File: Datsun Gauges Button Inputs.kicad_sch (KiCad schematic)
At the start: 13 parts, among them SW1 SW_Push, SW2 SW_Push, U1 4049, U2 4049

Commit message: Updated kicad diagrams
Updated kicad diagrams
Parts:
- removed D2: 1N4148, Diode_THT:D_DO-35_SOD27_P7.62mm_Horizontal, symbol Diode:1N4148
- added D2: 1N4734A 5.6v, Diode_THT:D_DO-41_SOD81_P10.16mm_Horizontal, symbol Diode:1N47xxA
- added D3: 1N4148, Diode_THT:D_DO-35_SOD27_P7.62mm_Horizontal, symbol Diode:1N4148
- R3, R4: value 10k -> 2k
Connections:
- net GND: now also D2.2 (A)
- net Park Brake Sw: now also D3.2 (A)
- net VCC: no longer R3.1
- net at C1.1, R4.1, U1.5: now also D2.1 (K), D3.1 (K)
- new net VDD: R3.1

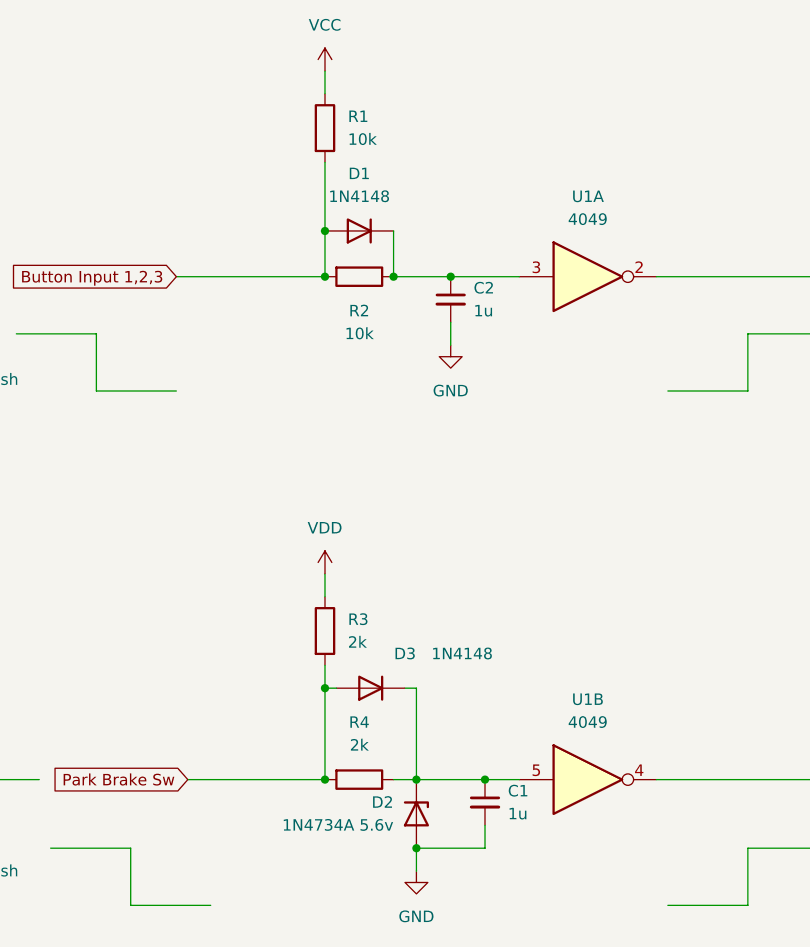
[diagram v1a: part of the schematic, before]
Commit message: Fixes
Changed some switch debouncing
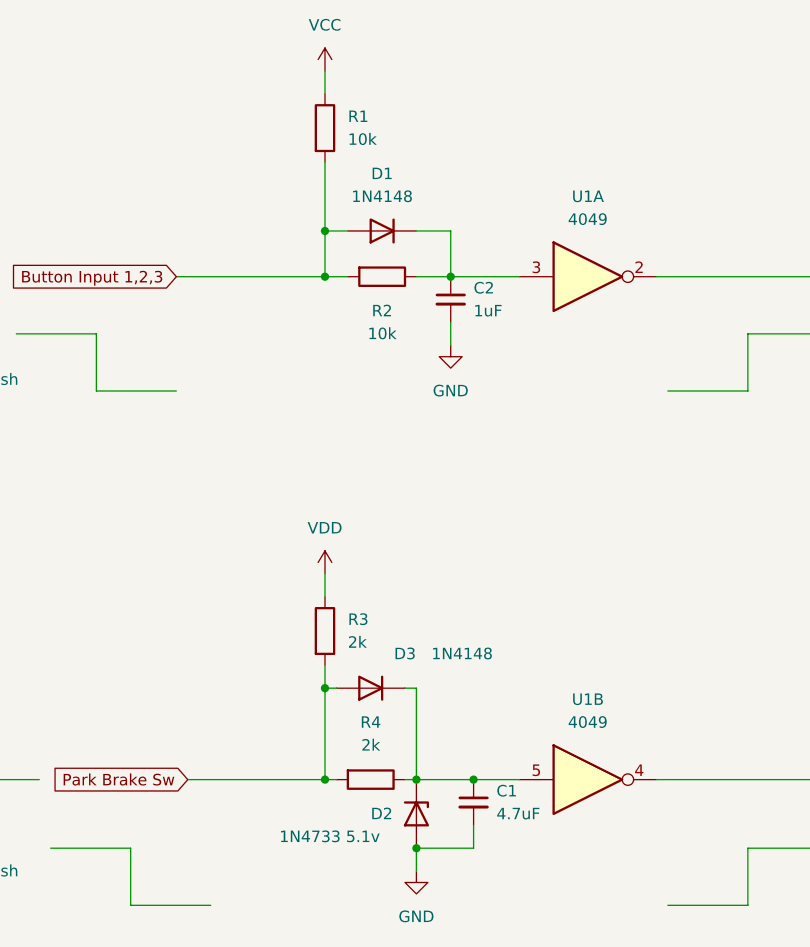
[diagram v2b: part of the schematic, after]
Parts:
- C1: value 1u -> 4.7uF
- C2: value 1u -> 1uF
- D2: value 1N4734A 5.6v -> 1N4733 5.1v
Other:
- moved on the sheet: C1, D1, R2, R4
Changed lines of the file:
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@@
   (junction (at 119.38 76.2) (diameter 0) (color 0 0 0 0)
   )
-  (junction (at 137.16 132.08) (diameter 0) (color 0 0 0 0)
-  )
   (junction (at 119.38 132.08) (diameter 0) (color 0 0 0 0)
   )
@@
   (junction (at 129.54 139.7) (diameter 0) (color 0 0 0 0)
   )
-  (junction (at 127 76.2) (diameter 0) (color 0 0 0 0)
+  (junction (at 135.89 132.08) (diameter 0) (color 0 0 0 0)
   )
   (junction (at 119.38 121.92) (diameter 0) (color 0 0 0 0)
@@
     (stroke (width 0) (type default))
   )
+  (wire (pts (xy 133.35 71.12) (xy 129.54 71.12))
+    (stroke (width 0) (type default))
+  )
   (wire (pts (xy 156.21 76.2) (xy 175.26 76.2))
     (stroke (width 0) (type default))
   )
-  (wire (pts (xy 137.16 137.16) (xy 137.16 139.7))
+  (wire (pts (xy 135.89 137.16) (xy 135.89 139.7))
     (stroke (width 0) (type default))
   )
@@
     (stroke (width 0) (type default) (color 0 0 255 1))
   )
-  (wire (pts (xy 127 71.12) (xy 127 76.2))
+  (wire (pts (xy 133.35 71.12) (xy 133.35 76.2))
     (stroke (width 0) (type default))
   )
@@
     (stroke (width 0) (type default) (color 0 0 255 1))
   )
-  (wire (pts (xy 127 132.08) (xy 129.54 132.08))
-    (stroke (width 0) (type default))
-  )
-  (wire (pts (xy 127 76.2) (xy 133.35 76.2))
-    (stroke (width 0) (type default))
-  )
   (wire (pts (xy 129.54 121.92) (xy 129.54 132.08))
     (stroke (width 0) (type default))
@@
     (stroke (width 0) (type default))
   )
+  (wire (pts (xy 135.89 132.08) (xy 140.97 132.08))
+    (stroke (width 0) (type default))
+  )
+  (wire (pts (xy 121.92 71.12) (xy 119.38 71.12))
+    (stroke (width 0) (type default))
+  )
+  (wire (pts (xy 133.35 76.2) (xy 129.54 76.2))
+    (stroke (width 0) (type default))
+  )
   (wire (pts (xy 228.6 34.29) (xy 228.6 25.4))
     (stroke (width 0) (type default))
@@
     (stroke (width 0) (type default))
   )
-  (wire (pts (xy 129.54 139.7) (xy 137.16 139.7))
+  (wire (pts (xy 129.54 139.7) (xy 135.89 139.7))
     (stroke (width 0) (type default))
   )
@@
     (stroke (width 0) (type default) (color 0 0 255 1))
   )
-  (wire (pts (xy 129.54 132.08) (xy 137.16 132.08))
+  (wire (pts (xy 129.54 132.08) (xy 135.89 132.08))
+    (stroke (width 0) (type default))
+  )
+  (wire (pts (xy 128.27 132.08) (xy 129.54 132.08))
     (stroke (width 0) (type default))
   )
@@
     (stroke (width 0) (type default))
   )
-  (wire (pts (xy 137.16 132.08) (xy 140.97 132.08))
+  (wire (pts (xy 121.92 76.2) (xy 119.38 76.2))
     (stroke (width 0) (type default))
   )
@@
   )
   (wire (pts (xy 119.38 109.22) (xy 119.38 111.76))
+    (stroke (width 0) (type default))
+  )
+  (wire (pts (xy 120.65 132.08) (xy 119.38 132.08))
     (stroke (width 0) (type default))
   )
@@
     )
   )
-  (symbol (lib_id "Device:C_Small") (at 137.16 134.62 0) (unit 1)
-    (in_bom yes) (on_board yes) (dnp no) (fields_autoplaced)
-    (property "Reference" "C1" (at 139.7 133.3563 0)
-      (effects (font (size 1.27 1.27)) (justify left))
-    )
-    (property "Value" "1u" (at 139.7 135.8963 0)
-      (effects (font (size 1.27 1.27)) (justify left))
-    )
-    (property "Footprint" "" (at 137.16 134.62 0)
-      (effects (font (size 1.27 1.27)) hide)
-    )
-    (property "Datasheet" "~" (at 137.16 134.62 0)
+  (symbol (lib_id "Device:C_Small") (at 135.89 134.62 0) (unit 1)
+    (in_bom yes) (on_board yes) (dnp no) (fields_autoplaced)
+    (property "Reference" "C1" (at 138.43 133.3563 0)
+      (effects (font (size 1.27 1.27)) (justify left))
+    )
+    (property "Value" "4.7uF" (at 138.43 135.8963 0)
+      (effects (font (size 1.27 1.27)) (justify left))
+    )
+    (property "Footprint" "" (at 135.89 134.62 0)
+      (effects (font (size 1.27 1.27)) hide)
+    )
+    (property "Datasheet" "~" (at 135.89 134.62 0)
       (effects (font (size 1.27 1.27)) hide)
     )
@@
   )
   (symbol (lib_id "Diode:1N47xxA") (at 129.54 135.89 270) (unit 1)
-    (in_bom yes) (on_board yes) (dnp no) (fields_autoplaced)
-    (property "Reference" "D2" (at 127 134.62 90)
-      (effects (font (size 1.27 1.27)) (justify right))
-    )
-    (property "Value" "1N4734A 5.6v" (at 127 137.16 90)
-      (effects (font (size 1.27 1.27)) (justify right))
+    (in_bom yes) (on_board yes) (dnp no)
+    (property "Reference" "D2" (at 124.46 135.89 90)
+      (effects (font (size 1.27 1.27)) (justify left))
+    )
+    (property "Value" "1N4733 5.1v" (at 114.3 138.43 90)
+      (effects (font (size 1.27 1.27)) (justify left))
     )
     (property "Footprint" "Diode_THT:D_DO-41_SOD81_P10.16mm_Horizontal" (at 125.095 135.89 0)
@@
       (effects (font (size 1.27 1.27)) (justify left))
     )
-    (property "Value" "1u" (at 135.89 80.0163 0)
+    (property "Value" "1uF" (at 135.89 80.0163 0)
       (effects (font (size 1.27 1.27)) (justify left))
     )
@@
     )
   )
-  (symbol (lib_id "Diode:1N4148") (at 123.19 71.12 180) (unit 1)
-    (in_bom yes) (on_board yes) (dnp no) (fields_autoplaced)
-    (property "Reference" "D1" (at 123.19 64.77 0)
-      (effects (font (size 1.27 1.27)))
-    )
-    (property "Value" "1N4148" (at 123.19 67.31 0)
-      (effects (font (size 1.27 1.27)))
-    )
-    (property "Footprint" "Diode_THT:D_DO-35_SOD27_P7.62mm_Horizontal" (at 123.19 71.12 0)
-      (effects (font (size 1.27 1.27)) hide)
-    )
-    (property "Datasheet" "https://assets.nexperia.com/documents/data-sheet/1N4148_1N4448.pdf" (at 123.19 71.12 0)
-      (effects (font (size 1.27 1.27)) hide)
-    )
-    (property "Sim.Device" "D" (at 123.19 71.12 0)
-      (effects (font (size 1.27 1.27)) hide)
-    )
-    (property "Sim.Pins" "1=K 2=A" (at 123.19 71.12 0)
+  (symbol (lib_id "Diode:1N4148") (at 125.73 71.12 180) (unit 1)
+    (in_bom yes) (on_board yes) (dnp no) (fields_autoplaced)
+    (property "Reference" "D1" (at 125.73 64.77 0)
+      (effects (font (size 1.27 1.27)))
+    )
+    (property "Value" "1N4148" (at 125.73 67.31 0)
+      (effects (font (size 1.27 1.27)))
+    )
+    (property "Footprint" "Diode_THT:D_DO-35_SOD27_P7.62mm_Horizontal" (at 125.73 71.12 0)
+      (effects (font (size 1.27 1.27)) hide)
+    )
+    (property "Datasheet" "https://assets.nexperia.com/documents/data-sheet/1N4148_1N4448.pdf" (at 125.73 71.12 0)
+      (effects (font (size 1.27 1.27)) hide)
+    )
+    (property "Sim.Device" "D" (at 125.73 71.12 0)
+      (effects (font (size 1.27 1.27)) hide)
+    )
+    (property "Sim.Pins" "1=K 2=A" (at 125.73 71.12 0)
       (effects (font (size 1.27 1.27)) hide)
     )
@@
     )
   )
-  (symbol (lib_id "Device:R") (at 123.19 76.2 270) (unit 1)
-    (in_bom yes) (on_board yes) (dnp no) (fields_autoplaced)
-    (property "Reference" "R2" (at 123.19 80.01 90)
-      (effects (font (size 1.27 1.27)))
-    )
-    (property "Value" "10k" (at 123.19 82.55 90)
-      (effects (font (size 1.27 1.27)))
-    )
-    (property "Footprint" "" (at 123.19 74.422 90)
-      (effects (font (size 1.27 1.27)) hide)
-    )
-    (property "Datasheet" "~" (at 123.19 76.2 0)
+  (symbol (lib_id "Device:R") (at 125.73 76.2 270) (unit 1)
+    (in_bom yes) (on_board yes) (dnp no) (fields_autoplaced)
+    (property "Reference" "R2" (at 125.73 80.01 90)
+      (effects (font (size 1.27 1.27)))
+    )
+    (property "Value" "10k" (at 125.73 82.55 90)
+      (effects (font (size 1.27 1.27)))
+    )
+    (property "Footprint" "" (at 125.73 74.422 90)
+      (effects (font (size 1.27 1.27)) hide)
+    )
+    (property "Datasheet" "~" (at 125.73 76.2 0)
       (effects (font (size 1.27 1.27)) hide)
     )
@@
     )
   )
-  (symbol (lib_id "Device:R") (at 123.19 132.08 270) (unit 1)
-    (in_bom yes) (on_board yes) (dnp no) (fields_autoplaced)
-    (property "Reference" "R4" (at 123.19 125.73 90)
-      (effects (font (size 1.27 1.27)))
-    )
-    (property "Value" "2k" (at 123.19 128.27 90)
-      (effects (font (size 1.27 1.27)))
-    )
-    (property "Footprint" "" (at 123.19 130.302 90)
-      (effects (font (size 1.27 1.27)) hide)
-    )
-    (property "Datasheet" "~" (at 123.19 132.08 0)
-      (effects (font (size 1.27 1.27)) hide)
-    )
+  (symbol (lib_id "Device:R") (at 124.46 132.08 270) (unit 1)
+    (in_bom yes) (on_board yes) (dnp no) (fields_autoplaced)
+    (property "Reference" "R4" (at 124.46 125.73 90)
+      (effects (font (size 1.27 1.27)))
+    )
+    (property "Value" "2k" (at 124.46 128.27 90)
+      (effects (font (size 1.27 1.27)))
+    )
+    (property "Footprint" "" (at 124.46 130.302 90)
+      (effects (font (size 1.27 1.27)) hide)
+    )
+    (property "Datasheet" "~" (at 124.46 132.08 0)
+      (effects (font (size 1.27 1.27)) hide)
+    )

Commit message: Cleanup
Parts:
- removed C1: 4.7uF, symbol Device:C_Small
- removed C2: 1uF, symbol Device:C_Small
- removed D2: 1N4733 5.1v, Diode_THT:D_DO-41_SOD81_P10.16mm_Horizontal, symbol Diode:1N47xxA
- added C1, C2: 4.7uF, symbol Device:C_Polarized_Small
- R1, R2: value 10k -> 8k2
- R3, R4: value 2k -> 8k2
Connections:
- net VDD is gone; now on net VCC: R3.1
- net GND: now also C1.2, C2.2
- net at D3.1 (K), R4.1, U1.5: now also C1.1
- net at D1.1 (K), R2.1, U1.3: now also C2.1
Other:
- moved on the sheet: D1, D3, R4
